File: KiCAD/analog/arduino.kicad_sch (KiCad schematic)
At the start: 56 parts, among them J10 Screw_Terminal_01x02, J12 Screw_Terminal_01x04, J13 Screw_Terminal_01x03, J14 Screw_Terminal_01x05, J16 Screw_Terminal_01x05, J2 8P8C_Shielded, J21 Screw_Terminal_01x02, J22 Screw_Terminal_01x04, J3 Screw_Terminal_01x04, J31 8P8C_Shielded, J32 Screw_Terminal_01x02, J35 8P8C_Shielded, J6 Screw_Terminal_01x02, J7 Screw_Terminal_01x02, J8 Screw_Terminal_01x02, J9 Screw_Terminal_01x02, Q10 2N7000, Q4 2N7000, Q5 2N7000, Q6 2N7000, Q7 2N7000, U17 Adafruit_PCF8575_Breakout, U18 CD14538B, U3 MCP4728

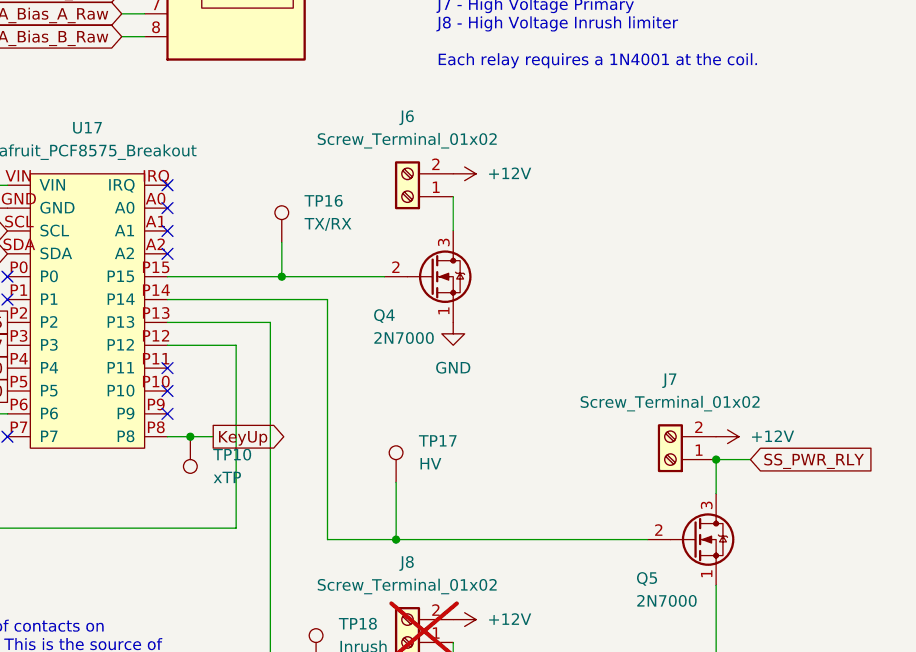
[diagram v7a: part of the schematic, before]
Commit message: revD analog: DGFET op-amp offset-mute topology + doc updates
Retire the Q11/Q12 PNP KeyUp mute path on the DGFET keyer G2 (sim showed
only ~2.6:1 on/off ratio with G1 biased above V_TO). Replace with an
LM7171 (U10) non-inverting op-amp wired as DC offset:
  V_G2 = V_DAC * (1 + R20/R23) - V_ref * (R20/R23)
with V_ref ~5.05V (1N4733A Zener D2, R24 1K bias, R25 1K / R32 100K
summing divider) and R20=6.2K / R23=10K (G=0.62). DAC=0 drives G2 to
-3.1V (fully cuts off the 40673, sim-verified 12pA leakage, ~10^9 on/off
ratio); DAC=5V drives G2 to +5V (matches prior keyed operating point).
KEY_UP net eliminated -- mute is intrinsic to the signal path, firmware
controls RF enable/disable solely via what it writes to the MCP4921
envelope channel.

Includes new test.kicad_sch sheet carrying the U10/R20-R32 subcircuit.

Doc updates: CLAUDE.md DGFET section rewritten; handoff doc gets a new
"DGFET keyer mute topology" section explaining retirement reason and
new transfer function; Master_Description Sec 2 and SPI-bus section
updated; revD_interconnect G2 amplitude-control block updated;
control_board_functional_blocks.md gets a prominent retirement banner
pointing at the current scheme.

Co-Authored-By: Claude Opus 4.7 <noreply@anthropic.com>
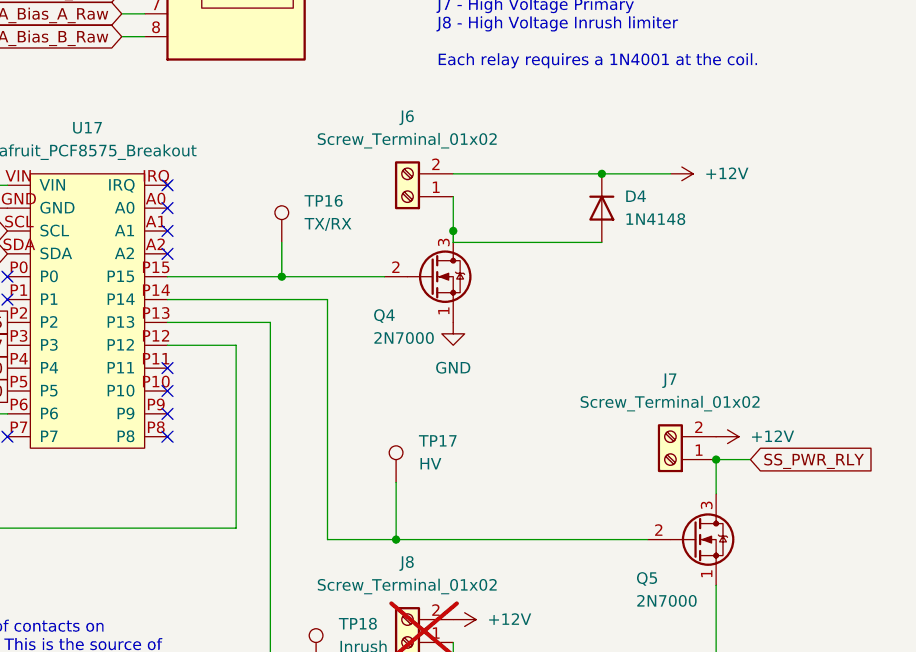
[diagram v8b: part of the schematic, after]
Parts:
- removed TP10: xTP, Connector_PinHeader_2.54mm:PinHeader_1x01_P2.54mm_Vertical, symbol xmitter:xTP
- added D4: 1N4148, Diode_THT:D_DO-35_SOD27_P7.62mm_Horizontal, symbol Diode:1N4148
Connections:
- net +12V: now also D4.1 (K)
- net KeyUp: no longer U17.P8
- net at J6.1 (Pin_1), Q4.3 (D): now also D4.2 (A)
- no-connect marks 16 -> 17
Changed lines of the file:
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@@
 	)
 	(junction
-		(at 195.58 86.36)
+		(at 90.17 127)
 		(diameter 0)
 		(color 0 0 0 0)
 	)
 	(junction
-		(at 90.17 127)
+		(at 254 88.9)
 		(diameter 0)
 		(color 0 0 0 0)
 	)
 	(junction
-		(at 254 88.9)
+		(at 78.74 121.92)
 		(diameter 0)
 		(color 0 0 0 0)
 	)
 	(junction
-		(at 78.74 121.92)
+		(at 241.3 57.15)
 		(diameter 0)
 		(color 0 0 0 0)
@@
 	)
 	(junction
+		(at 224.79 63.5)
+		(diameter 0)
+		(color 0 0 0 0)
+	)
+	(junction
 		(at 171.45 29.21)
 		(diameter 0)
@@
 	)
 	(no_connect
+		(at 193.04 86.36)
+	)
+	(no_connect
 		(at 175.26 71.12)
 	)
@@
 	(wire
 		(pts
+			(xy 241.3 57.15) (xy 248.92 57.15)
+		)
+		(stroke
+			(width 0)
+			(type default)
+		)
+	)
+	(wire
+		(pts
 			(xy 193.04 71.12) (xy 210.82 71.12)
 		)
@@
 	(wire
 		(pts
+			(xy 224.79 57.15) (xy 241.3 57.15)
+		)
+		(stroke
+			(width 0)
+			(type default)
+		)
+	)
+	(wire
+		(pts
 			(xy 205.74 64.77) (xy 205.74 68.58)
 		)
@@
 	(wire
 		(pts
+			(xy 224.79 63.5) (xy 224.79 64.77)
+		)
+		(stroke
+			(width 0)
+			(type default)
+		)
+	)
+	(wire
+		(pts
 			(xy 191.77 142.24) (xy 191.77 152.4)
 		)
@@
 	(wire
 		(pts
-			(xy 195.58 86.36) (xy 193.04 86.36)
+			(xy 68.58 127) (xy 78.74 127)
 		)
 		(stroke
@@
 	(wire
 		(pts
-			(xy 68.58 127) (xy 78.74 127)
+			(xy 241.3 64.77) (xy 224.79 64.77)
 		)
 		(stroke
@@
 	(wire
 		(pts
-			(xy 198.12 86.36) (xy 195.58 86.36)
-		)
-		(stroke
-			(width 0)
-			(type default)
-		)
-	)
-	(wire
-		(pts
 			(xy 68.58 121.92) (xy 78.74 121.92)
 		)
@@
 		)
 	)
-	(global_label "KeyUp"
-		(shape output)
-		(at 198.12 86.36 0)
-		(fields_autoplaced yes)
-		(effects
-			(font
-				(size 1.27 1.27)
-			)
-			(justify left)
-		)
-		(property "Intersheetrefs" "${INTERSHEET_REFS}"
-			(at 206.9109 86.36 0)
-			(hide yes)
-			(show_name no)
-			(do_not_autoplace no)
-			(effects
-				(font
-					(size 1.27 1.27)
-				)
-				(justify left)
-			)
-		)
-	)
 	(global_label "PA_Bias_B_Raw"
 		(shape output)
@@
 	)
 	(symbol
+		(lib_id "Diode:1N4148")
+		(at 241.3 60.96 270)
+		(unit 1)
+		(body_style 1)
+		(exclude_from_sim no)
+		(in_bom yes)
+		(on_board yes)
+		(in_pos_files yes)
+		(dnp no)
+		(fields_autoplaced yes)
+		(property "Reference" "D4"
+			(at 243.84 59.6899 90)
+			(show_name no)
+			(do_not_autoplace no)
+			(effects
+				(font
+					(size 1.27 1.27)
+				)
+				(justify left)
+			)
+		)
+		(property "Value" "1N4148"
+			(at 243.84 62.2299 90)
+			(show_name no)
+			(do_not_autoplace no)
+			(effects
+				(font
+					(size 1.27 1.27)
+				)
+				(justify left)
+			)
+		)
+		(property "Footprint" "Diode_THT:D_DO-35_SOD27_P7.62mm_Horizontal"
+			(at 241.3 60.96 0)
+			(hide yes)
+			(show_name no)
+			(do_not_autoplace no)
+			(effects
+				(font
+					(size 1.27 1.27)
+				)
+			)
+		)
+		(property "Datasheet" "https://assets.nexperia.com/documents/data-sheet/1N4148_1N4448.pdf"
+			(at 241.3 60.96 0)
+			(hide yes)
+			(show_name no)
+			(do_not_autoplace no)
+			(effects
+				(font
+					(size 1.27 1.27)
+				)
+			)
+		)
+		(property "Description" "100V 0.15A standard switching diode, DO-35"
+			(at 241.3 60.96 0)
+			(hide yes)
+			(show_name no)
+			(do_not_autoplace no)
+			(effects
+				(font
+					(size 1.27 1.27)
+				)
+			)
+		)
+		(property "Sim.Device" "D"
+			(at 241.3 60.96 0)
+			(hide yes)
+			(show_name no)
+			(do_not_autoplace no)
+			(effects
+				(font
+					(size 1.27 1.27)
+				)
+			)
+		)
+		(property "Sim.Pins" "1=K 2=A"
+			(at 241.3 60.96 0)
+			(hide yes)
+			(show_name no)
+			(do_not_autoplace no)
+			(effects
+				(font
+					(size 1.27 1.27)
+				)
+			)
+		)
+		(pin "1"
+		)
+		(pin "2"
+		)
+		(instances
+			(project "analog"
+				(path "/d3de40b8-856b-4fbd-829c-f45ffcd55742/2d83d0b5-86d4-4ced-ab68-6465e3dc2d72"
+					(reference "D4")
+					(unit 1)
+				)
+			)
+		)
+	)
+	(symbol
 		(lib_id "Device:R_US")
 		(at 64.77 66.04 270)
@@
 	)
 	(symbol
-		(lib_id "xmitter:xTP")
-		(at 195.58 86.36 180)
-		(unit 1)
-		(body_style 1)
-		(exclude_from_sim no)
-		(in_bom yes)
-		(on_board yes)
-		(in_pos_files yes)
-		(dnp no)
-		(fields_autoplaced yes)
-		(property "Reference" "TP10"
-			(at 198.12 88.3919 0)
-			(show_name no)
-			(do_not_autoplace no)
-			(effects
-				(font
-					(size 1.27 1.27)
-				)
-				(justify right)
-			)
-		)
-		(property "Value" "xTP"
-			(at 198.12 90.9319 0)
-			(show_name no)
-			(do_not_autoplace no)
-			(effects
-				(font
-					(size 1.27 1.27)
-				)
-				(justify right)
-			)
-		)
-		(property "Footprint" "Connector_PinHeader_2.54mm:PinHeader_1x01_P2.54mm_Vertical"
-			(at 190.5 86.36 0)
-			(hide yes)
-			(show_name no)
-			(do_not_autoplace no)
-			(effects
-				(font
-					(size 1.27 1.27)
-				)
-			)
-		)
-		(property "Datasheet" ""
-			(at 190.5 86.36 0)
-			(hide yes)
-			(show_name no)
-			(do_not_autoplace no)
-			(effects
-				(font
-					(size 1.27 1.27)
-				)
-			)
-		)
-		(property "Description" "xmitter project test point on broken-off 0.1 inch square pin header; put signal name in Value field so it becomes silk on the PCB"
-			(at 195.58 86.36 0)
-			(hide yes)
-			(show_name no)
-			(do_not_autoplace no)
-			(effects
-				(font
-					(size 1.27 1.27)
-				)
-			)
-		)
-		(pin "1"
-		)
-		(instances
-			(project "analog"
-				(path "/d3de40b8-856b-4fbd-829c-f45ffcd55742/2d83d0b5-86d4-4ced-ab68-6465e3dc2d72"
-					(reference "TP10")
-					(unit 1)
-				)
-			)
-		)
-	)
-	(symbol
 		(lib_id "Connector:Screw_Terminal_01x05")
 		(at 25.4 113.03 180)
@@
 	(symbol
 		(lib_id "power:+12V")
-		(at 224.79 57.15 270)
+		(at 248.92 57.15 270)
 		(unit 1)
 		(body_style 1)
@@
 		(fields_autoplaced yes)
 		(property "Reference" "#PWR0107"
-			(at 220.98 57.15 0)
+			(at 245.11 57.15 0)
 			(hide yes)
 			(show_name no)
@@
 		)
 		(property "Value" "+12V"
-			(at 228.6 57.1499 90)
+			(at 252.73 57.1499 90)
 			(show_name no)
 			(do_not_autoplace no)
@@
 		)
 		(property "Footprint" ""
-			(at 224.79 57.15 0)
+			(at 248.92 57.15 0)
 			(hide yes)
 			(show_name no)
@@
 		)
 		(property "Datasheet" ""
-			(at 224.79 57.15 0)
+			(at 248.92 57.15 0)
 			(hide yes)
 			(show_name no)
@@
 		)
 		(property "Description" "Power symbol creates a global label with name \"+12V\""
-			(at 224.79 57.15 0)
+			(at 248.92 57.15 0)
 			(hide yes)
 			(show_name no)
